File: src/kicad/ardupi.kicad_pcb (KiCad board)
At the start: 2 copper layers, 65 x 56 mm, 69 parts, among them J1 RPI-4B-Header, J2 Conn_01x10, J3 Conn_01x05, J4 Conn_01x04, J6 Conn_01x05, J7 Conn_01x06, J8 Conn_01x04, J9 Conn_01x02, M1 NEO-M8Q-01A, U1 CAT24C32WI-GT3, U2 ULN2803ADWR, U3 PCA9685PW, U4 ADS1115IDGSR, U5 MPU-9250, U6 BMP280, U7 RFM95W-868S2

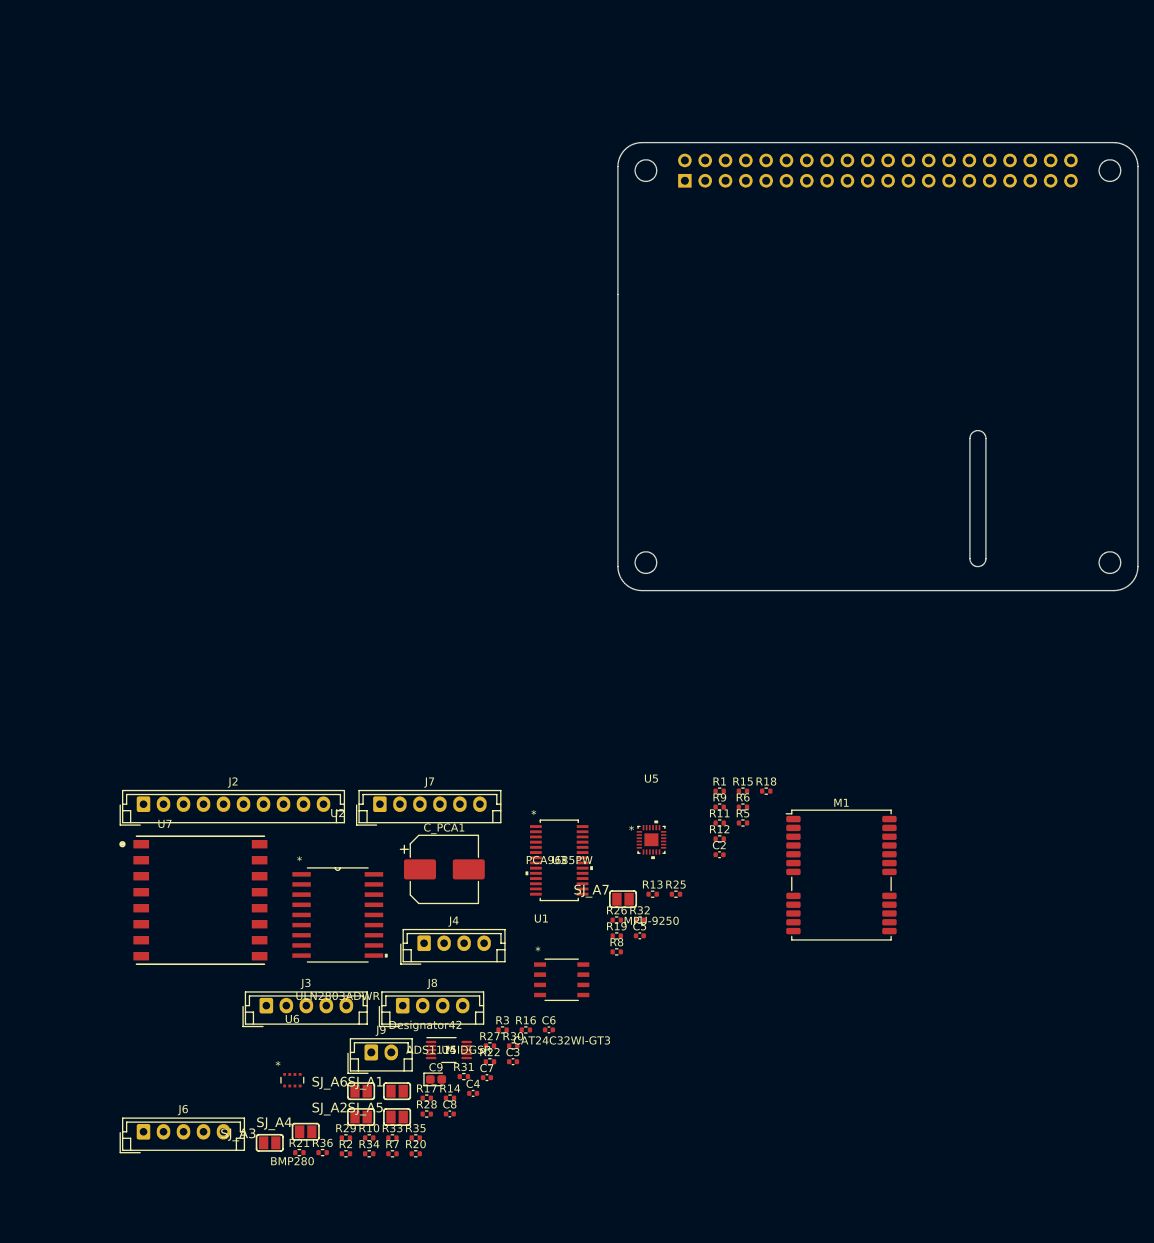
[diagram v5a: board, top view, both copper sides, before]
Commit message: update all symbols & footprints.
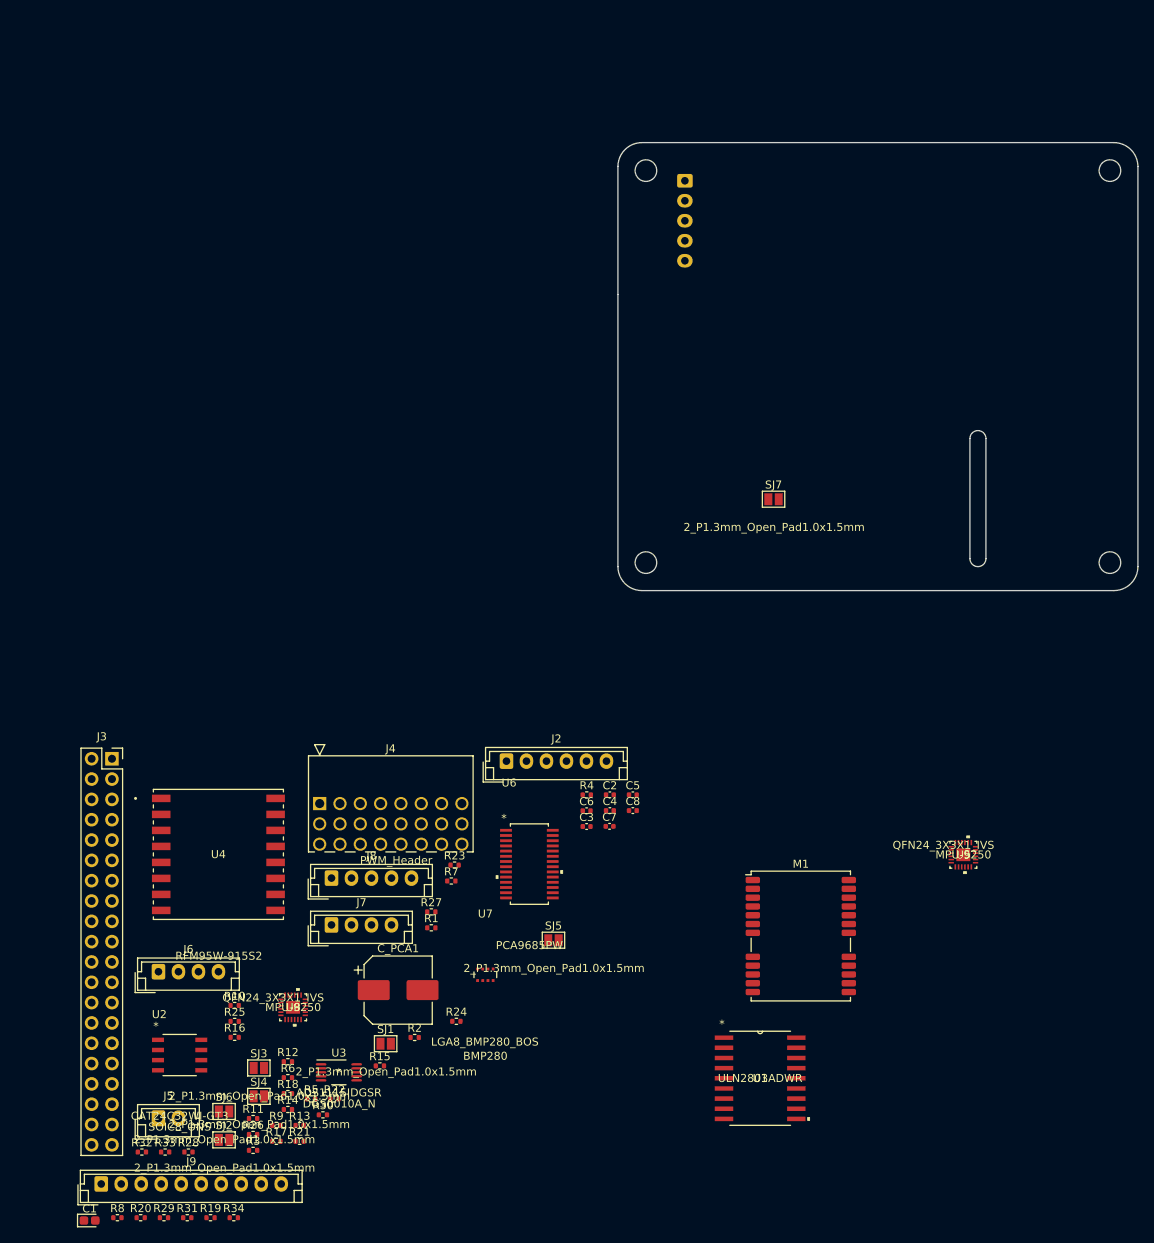
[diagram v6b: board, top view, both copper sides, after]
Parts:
- removed C9: 100n, Capacitor_Tantalum_SMD:CP_EIA-1608-10_AVX-L
- removed R35: 4.7KΩ, Resistor_SMD:R_0402_1005Metric
- removed R36: 10KΩ, Resistor_SMD:R_0402_1005Metric
- removed SJ_A1, SJ_A2, SJ_A3, SJ_A4, SJ_A5, SJ_A6, SJ_A7: SOLDERJUMPERREFLOW_NOPASTE, Ardupi:SOLDERJUMPER_REFLOW_NOPASTE
- added C1: 100n, Capacitor_Tantalum_SMD:CP_EIA-1608-10_AVX-L, F.Cu at (34.0, 178.7)
- added J5: Conn_01x02, Connector_JST:JST_EH_B2B-EH-A_1x02_P2.50mm_Vertical, F.Cu at (42.6, 166.0)
- added R23: 220 Ω, Resistor_SMD:R_0402_1005Metric, F.Cu at (79.6, 134.3)
- added R24: 10KΩ, Resistor_SMD:R_0402_1005Metric, F.Cu at (79.8, 153.8)
- added R4: 10K, Resistor_SMD:R_0402_1005Metric, F.Cu at (96.1, 125.5)
- added SJ1: SolderJumper-Open_Pad, Ardupi:SolderJumper-Open_Pad, F.Cu at (71.0, 156.6)
- added SJ2: SolderJumper-Open_Pad, Ardupi:SolderJumper-Open_Pad, F.Cu at (50.8, 168.7)
- added SJ3: SolderJumper-Open_Pad, Ardupi:SolderJumper-Open_Pad, F.Cu at (55.1, 159.7)
- added SJ4: SolderJumper-Open_Pad, Ardupi:SolderJumper-Open_Pad, F.Cu at (55.1, 163.2)
- added SJ5: SolderJumper-Open_Pad, Ardupi:SolderJumper-Open_Pad, F.Cu at (91.9, 143.7)
- added SJ6: SolderJumper-Open_Pad, Ardupi:SolderJumper-Open_Pad, F.Cu at (50.8, 165.1)
- added SJ7: SolderJumper-Open_Pad, Ardupi:SolderJumper-Open_Pad, F.Cu at (119.5, 88.6)
- added U8: MPU-9250, Ardupi:MPU-9250, F.Cu at (59.4, 152.1)
- C2: value 0.1uF -> 1uF
- C3: value 1uF -> 0.1uf
- C4: value 1uF -> 0.1uF
- C5: value 0.1uf -> 0.1uF
- C6: value 0.1uF -> 0.01uF
- C7: value 0.01uF -> 1uF
- J1: value RPI-4B-Header -> Conn_01x05; footprint Connector_PinSocket_2.54mm:PinSocket_2x20_P2.54mm_Vertical -> Connector_JST:JST_EH_B5B-EH-A_1x05_P2.50mm_Vertical
- J2: value Conn_01x10 -> Conn_01x06; footprint Connector_JST:JST_EH_B10B-EH-A_1x10_P2.50mm_Vertical -> Connector_JST:JST_EH_B6B-EH-A_1x06_P2.50mm_Vertical
- J3: value Conn_01x05 -> RPI-4B-Header; footprint Connector_JST:JST_EH_B5B-EH-A_1x05_P2.50mm_Vertical -> Connector_PinSocket_2.54mm:PinSocket_2x20_P2.54mm_Vertical
- J4: value Conn_01x04 -> PWM_Header; footprint Connector_JST:JST_EH_B4B-EH-A_1x04_P2.50mm_Vertical -> Ardupi:PWM_Header
- J6: value Conn_01x05 -> Conn_01x04; footprint Connector_JST:JST_EH_B5B-EH-A_1x05_P2.50mm_Vertical -> Connector_JST:JST_EH_B4B-EH-A_1x04_P2.50mm_Vertical
- J7: value Conn_01x06 -> Conn_01x04; footprint Connector_JST:JST_EH_B6B-EH-A_1x06_P2.50mm_Vertical -> Connector_JST:JST_EH_B4B-EH-A_1x04_P2.50mm_Vertical
- J8: value Conn_01x04 -> Conn_01x05; footprint Connector_JST:JST_EH_B4B-EH-A_1x04_P2.50mm_Vertical -> Connector_JST:JST_EH_B5B-EH-A_1x05_P2.50mm_Vertical
- J9: value Conn_01x02 -> Conn_01x10; footprint Connector_JST:JST_EH_B2B-EH-A_1x02_P2.50mm_Vertical -> Connector_JST:JST_EH_B10B-EH-A_1x10_P2.50mm_Vertical
- R11: value 10K -> 1k
- R12: value 460 -> 3.9k
- R13: value 220 Ω -> 3.9k
- R14, R15: value 220 Ω -> 10KΩ
- R2: value 10k -> 10K
- R21, R22: value 3.9k -> 220 Ω
- R26: value 10KΩ -> 10K
- R27: value 10KΩ -> 460
- R28: value 10KΩ -> 4.7KΩ
- R3: value 1k -> 10K
- R33, R34: value 4.7KΩ -> 10KΩ
- R6, R8: value 10K -> 10k
- R7: value 10K -> 10KΩ
- R9: value 10k -> 10KΩ
- U1: value CAT24C32WI-GT3 -> ULN2803ADWR; footprint Ardupi:CAT24C32WI-GT3 -> Ardupi:ULN2803ADWR
- U2: value ULN2803ADWR -> CAT24C32WI-GT3; footprint Ardupi:ULN2803ADWR -> Ardupi:CAT24C32WI-GT3
- U3: value PCA9685PW -> ADS1115IDGSR; footprint Ardupi:PCA9685PW_118 -> Ardupi:ADS1115IDGSR
- U4: value ADS1115IDGSR -> RFM95W-915S2; footprint Ardupi:ADS1115IDGSR -> Ardupi:RFM95W-915S2
- U5: footprint Ardupi:mpu9250 -> Ardupi:MPU-9250
- U6: value BMP280 -> PCA9685PW; footprint Ardupi:bmp280 -> Ardupi:PCA9685PW
- U7: value RFM95W-868S2 -> BMP280; footprint Ardupi:RFM95W-868S2 -> Ardupi:BMP280
- moved R18 70.7 mm to (58.7, 162.9)
- moved R8 70.7 mm to (37.4, 178.4)
- moved R11 69.0 mm to (54.4, 166.0)
- moved R32 68.7 mm to (40.5, 170.2)
- moved R9 68.2 mm to (57.3, 166.8)
- moved R6 66.2 mm to (58.7, 160.9)
- moved R5 64.1 mm to (61.7, 163.5)
- moved R19 61.8 mm to (49.1, 178.4)
- moved R12 60.7 mm to (58.7, 158.9)
- moved R25 57.4 mm to (52.1, 153.8)
- moved R15 56.9 mm to (70.2, 159.4)
- moved R26 52.8 mm to (54.4, 168.0)
- moved R13 52.7 mm to (60.2, 166.8)
- moved J2 45.7 mm to (86.1, 121.3)
- moved C8 44.3 mm to (101.9, 127.5)
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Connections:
- C2 pad 1: +3V3 -> +5V
- C3 pad 1: +3V3 -> +5V
- C4 pad 1: +5V -> Net-(C4-Pad1)
- C5 pad 1: +5V -> +3V3
- C6 pad 1: Net-(C6-Pad1) -> +3V3
- J1 pad 1: +3V3 -> /BUZZER_OUT
- J1 pad 2: +5V -> /LED1_OUT
- J1 pad 3: /SDA1 -> /LED2_OUT
- J1 pad 4: +5V -> /LED3_OUT
- J1 pad 5: /SCL1 -> V_EXT
- J2 pad 1: GND -> /AIO3
- J2 pad 2: +5V -> /AIO2
- J2 pad 3: /RC1 -> /AIO1
- J2 pad 4: /RC2 -> /AIO0
- J2 pad 5: /RC3 -> GND
- J2 pad 6: /RC4 -> GND
- J3 pad 1: GND -> +3V3
- J3 pad 3: /MOSI -> /SDA1
- J3 pad 4: /MISO -> +5V
- J3 pad 5: /SCLK -> /SCL1
- J4 pad 1: +5V -> Net-(J4-Pad1)
- J4 pad 2: GND -> V_EXT
- J4 pad 3: /TX -> GND
- J4 pad 4: /RX -> Net-(J4-Pad4)
- J6 pad 1: /BUZZER_OUT -> +5V
- J6 pad 2: /LED1_OUT -> GND
- J6 pad 3: /LED2_OUT -> /TX
- J6 pad 4: /LED3_OUT -> /RX
- J7 pad 1: /AIO3 -> +5V
- J7 pad 2: /AIO2 -> /SDA
- J7 pad 3: /AIO1 -> /SCL
- J7 pad 4: /AIO0 -> GND
- J8 pad 1: +5V -> GND
- J8 pad 2: /SDA -> +5V
- J8 pad 3: /SCL -> /MOSI
- J8 pad 4: GND -> /MISO
- J9 pad 1: /SRVO_EN -> GND
- J9 pad 2: Net-(J9-Pad2) -> +5V
- R1 pad 1: +5V -> Net-(R1-Pad1)
- R1 pad 2: /SCL1 -> GND
- R10 pad 1: Net-(R10-Pad1) -> +5V
- R10 pad 2: GND -> /SDA1
- R11 pad 1: +5V -> Net-(R11-Pad1)
- R11 pad 2: Net-(J9-Pad2) -> +3V3
- R12 pad 1: /PCA_EN -> /ID_SD
- R12 pad 2: Net-(J9-Pad2) -> +3V3
- R13 pad 1: Net-(J5-Pad1) -> +3V3
- R13 pad 2: /PWM1 -> /ID_SC
- R14 pad 1: Net-(J5-Pad4) -> /SCL1
- R14 pad 2: /PWM2 -> +5V
- R15 pad 1: Net-(J5-Pad7) -> +5V
- R15 pad 2: /PWM3 -> /SDA1
- R16 pad 1: Net-(J5-Pad10) -> Net-(J4-Pad1)
- R16 pad 2: /PWM4 -> /PWM1
- R17 pad 1: /PWM8 -> Net-(J4-Pad4)
- R17 pad 2: Net-(J5-Pad22) -> /PWM2
- R18 pad 1: /PWM7 -> Net-(J4-Pad7)
- R18 pad 2: Net-(J5-Pad19) -> /PWM3
- R19 pad 1: /PWM6 -> Net-(J4-Pad10)
- R19 pad 2: Net-(J5-Pad16) -> /PWM4
- R2 pad 1: +5V -> Net-(R2-Pad1)
- R2 pad 2: /SDA1 -> GND
- R20 pad 1: /PWM5 -> /PWM8
- R20 pad 2: Net-(J5-Pad13) -> Net-(J4-Pad22)
- R21 pad 1: /ID_SD -> /PWM7
- R21 pad 2: +3V3 -> Net-(J4-Pad19)
- R22 pad 1: +3V3 -> /PWM6
- R22 pad 2: /ID_SC -> Net-(J4-Pad16)
- R25 pad 1: Net-(R25-Pad1) -> GND
- R25 pad 2: +5V -> Net-(R25-Pad2)
- R26 pad 1: /SPI_MISO -> +5V
- R26 pad 2: GND -> Net-(J5-Pad2)
- R27 pad 1: Net-(R27-Pad1) -> /PCA_EN
- R27 pad 2: +5V -> Net-(J5-Pad2)
- R28 pad 1: /SPI_MOSI -> +3V3
- R28 pad 2: +3V3 -> /SPI_CE1_N
- R29 pad 1: /SPI_SCLK -> +3V3
- R29 pad 2: +3V3 -> /SPI_MOSI
- R3 pad 2: +3V3 -> GND
- R30 pad 1: /SPI_CE0_N -> +3V3
- R30 pad 2: +3V3 -> /SPI_SCLK
- R31 pad 1: /SCL1 -> /SPI_MOSI
- R31 pad 2: +5V -> +3V3
- R32 pad 1: +5V -> /SPI_MISO
- R32 pad 2: /SDA1 -> GND
- R33 pad 1: +3V3 -> /SPI_SCLK
- R33 pad 2: /SPI_CE1_N -> +3V3
- R34 pad 1: +3V3 -> /SPI_CE0_N
- R34 pad 2: /SPI_MOSI -> +3V3
- R7 pad 2: GND -> +5V
- R8 pad 1: Net-(R8-Pad1) -> +5V
- R8 pad 2: GND -> /SCL1
- R9 pad 2: GND -> +5V
- U1 pad 1: GND -> /BUZZER
- U1 pad 2: GND -> /BUZZER
- U1 pad 3: GND -> /LED1
- U1 pad 4: GND -> /LED1
- U1 pad 5: /ID_SD -> /LED2
- U1 pad 6: /ID_SC -> /LED2
- U1 pad 7: Net-(R3-Pad1) -> /LED3
- U1 pad 8: +3V3 -> /LED3
- U2 pad 1: /BUZZER -> GND
- U2 pad 2: /BUZZER -> GND
- U2 pad 3: /LED1 -> GND
- U2 pad 4: /LED1 -> GND
- U2 pad 5: /LED2 -> /ID_SD
- U2 pad 6: /LED2 -> /ID_SC
- U2 pad 7: /LED3 -> Net-(R11-Pad1)
- U2 pad 8: /LED3 -> +3V3
- U3 pad 1: Net-(R5-Pad1) -> Net-(R9-Pad1)
- U3 pad 10: /PWM5 -> /AIO2
- U3 pad 2: Net-(R6-Pad1) -> Net-(R7-Pad1)
- U3 pad 3: Net-(R7-Pad1) -> GND
- U3 pad 4: Net-(R8-Pad1) -> /AIO0
- U3 pad 5: Net-(R9-Pad1) -> /AIO1
- U3 pad 6: /PWM1 -> /SCL1
- U3 pad 7: /PWM2 -> /SDA1
- U3 pad 8: /PWM3 -> +5V
- U3 pad 9: /PWM4 -> /AIO3
- U4 pad 1: Net-(R27-Pad1) -> unconnected-(U4-Pad1)
- U4 pad 10: /AIO2 -> unconnected-(U4-Pad10)
- U4 pad 2: Net-(R25-Pad1) -> unconnected-(U4-Pad2)
- U4 pad 3: GND -> unconnected-(U4-Pad3)
- U4 pad 4: /AIO0 -> unconnected-(U4-Pad4)
- U4 pad 5: /AIO1 -> unconnected-(U4-Pad5)
- U4 pad 6: /SCL1 -> unconnected-(U4-Pad6)
- U4 pad 7: /SDA1 -> unconnected-(U4-Pad7)
- U4 pad 8: +5V -> unconnected-(U4-Pad8)
- U4 pad 9: /AIO3 -> unconnected-(U4-Pad9)
- U5 pad 1: unconnected-(U5-Pad1) -> +3V3
- U5 pad 10: Net-(C6-Pad1) -> Net-(C4-Pad1)
- U5 pad 11: GND -> Net-(R25-Pad2)
- U6 pad 1: GND -> Net-(R1-Pad1)
- U6 pad 2: /SPI_CE1_N -> Net-(R2-Pad1)
- U6 pad 3: /SPI_MOSI -> Net-(R3-Pad1)
- U6 pad 4: /SPI_SCLK -> Net-(R4-Pad1)
- U6 pad 5: /SPI_MISO -> Net-(R5-Pad1)
- U6 pad 6: +3V3 -> /PWM1
- U6 pad 7: GND -> /PWM2
- U6 pad 8: +3V3 -> /PWM3
- U7 pad 1: GND -> unconnected-(U7-Pad1)
- U7 pad 2: unconnected-(U7-Pad2) -> GND
- U7 pad 3: unconnected-(U7-Pad3) -> /SPI_CE1_N
- U7 pad 4: unconnected-(U7-Pad4) -> /SPI_MOSI
- U7 pad 5: unconnected-(U7-Pad5) -> +3V3
- U7 pad 6: unconnected-(U7-Pad6) -> GND
- U7 pad 7: unconnected-(U7-Pad7) -> +3V3
- U7 pad 8: GND -> unconnected-(U7-Pad8)
